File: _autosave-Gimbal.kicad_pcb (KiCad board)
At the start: 2 copper layers, 68.6 x 78.7 mm, 53 parts, among them J1 XT60-M, J3 0022232041, J4 0022232041, J5 0022232041, J6 Conn_01x02, P1 USB_C_Plug, SW1 SW_Push, SW2 SW_Push, U1 ESP32-S2-SOLO, U2 BMI088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

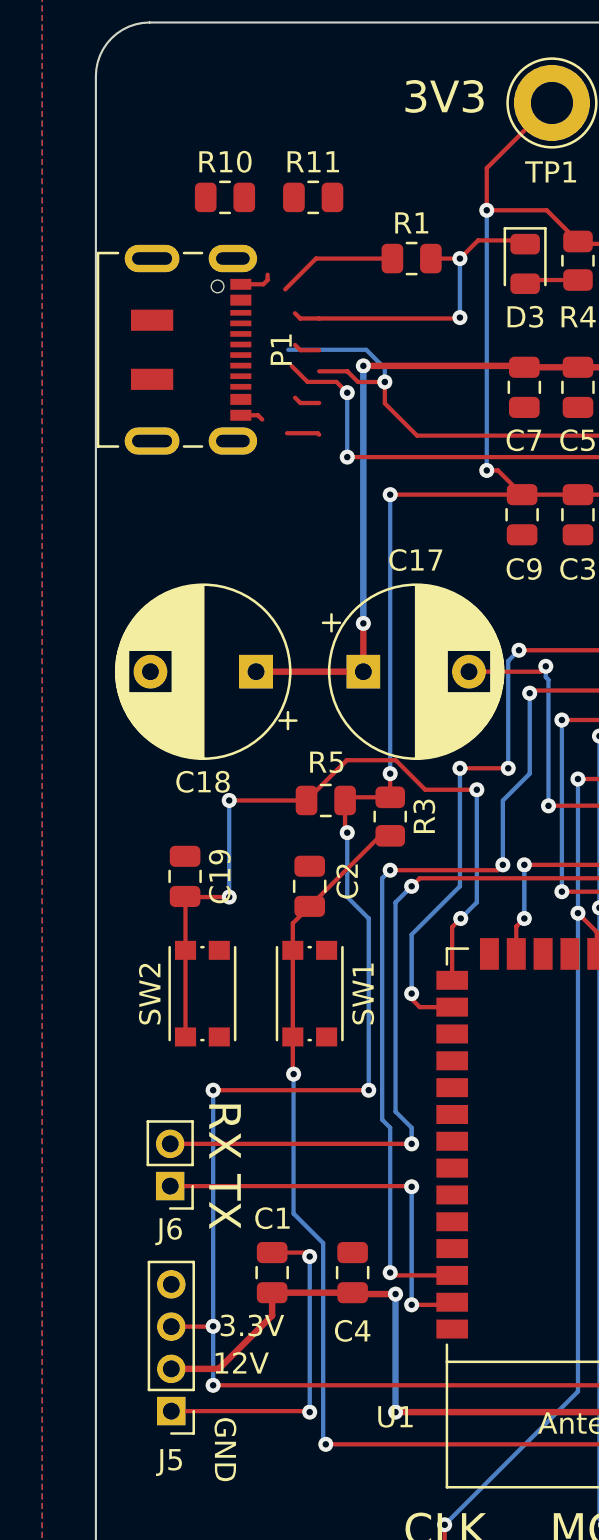
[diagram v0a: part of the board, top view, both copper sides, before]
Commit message: Fixed USB connector issues
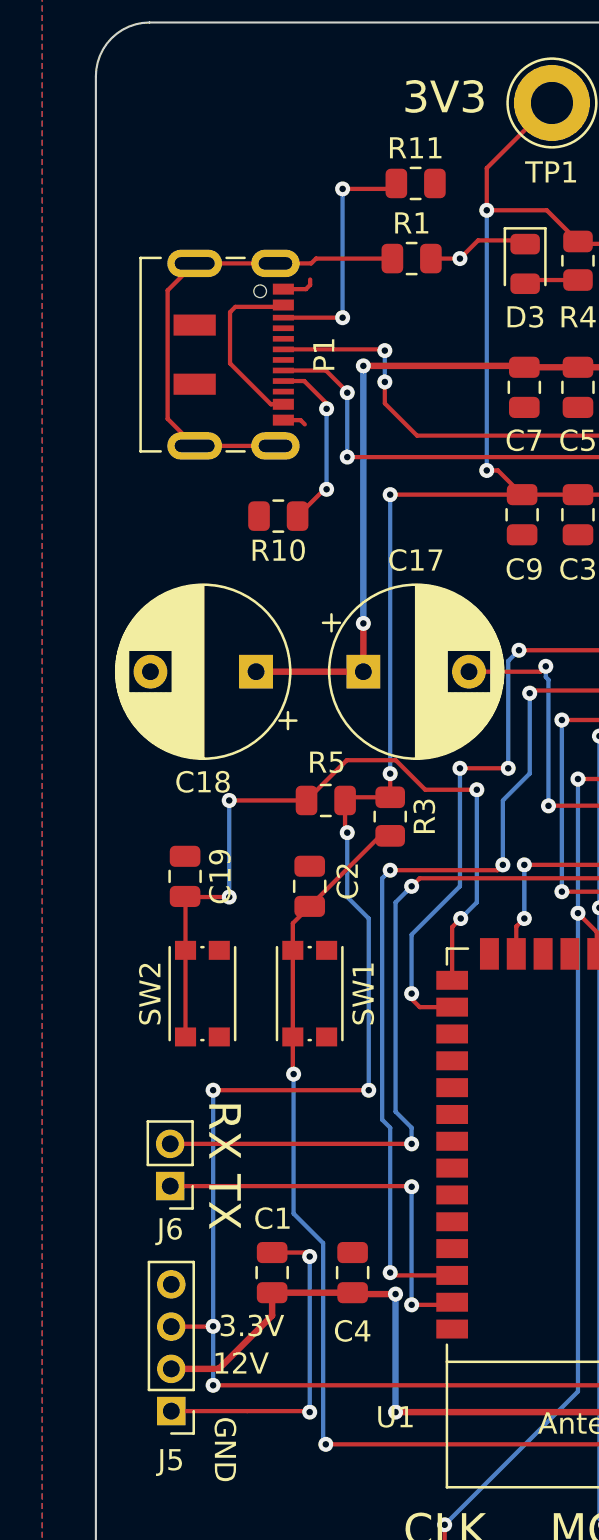
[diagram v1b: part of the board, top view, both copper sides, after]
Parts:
- moved R10 15.3 mm to (122.9, 69.1), turned to 180 degrees
- moved R11 4.89 mm to (129.4, 53.3)
- moved P1 2.03 mm to (120.1, 61.4)
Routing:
- net Net-(R1-Pad1): track 5.68 -> 23.0 mm
- net GND: track 60.2 -> 45.4 mm, vias 8 -> 7
- net Net-(R11-Pad1): track 0.00 -> 11.6 mm, vias 0 -> 2
- net Net-(R10-Pad1): track 0.00 -> 8.45 mm, vias 0 -> 2
- net unconnected-(P1-PadA4): track 0.00 -> 8.42 mm
- net /D+: track 58.5 -> 55.9 mm, vias 3 -> 4

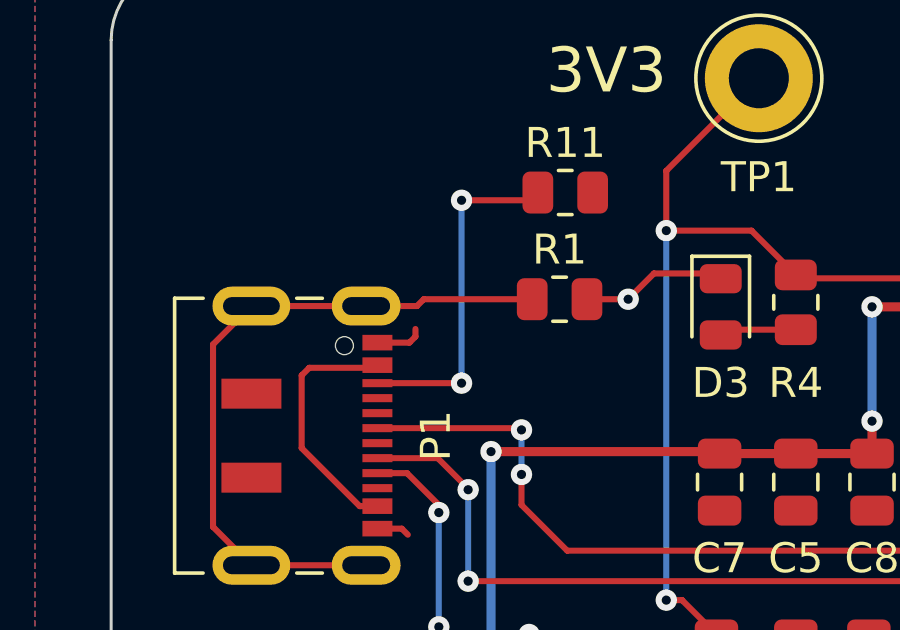
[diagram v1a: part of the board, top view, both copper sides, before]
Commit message: Fixed USB connector issues
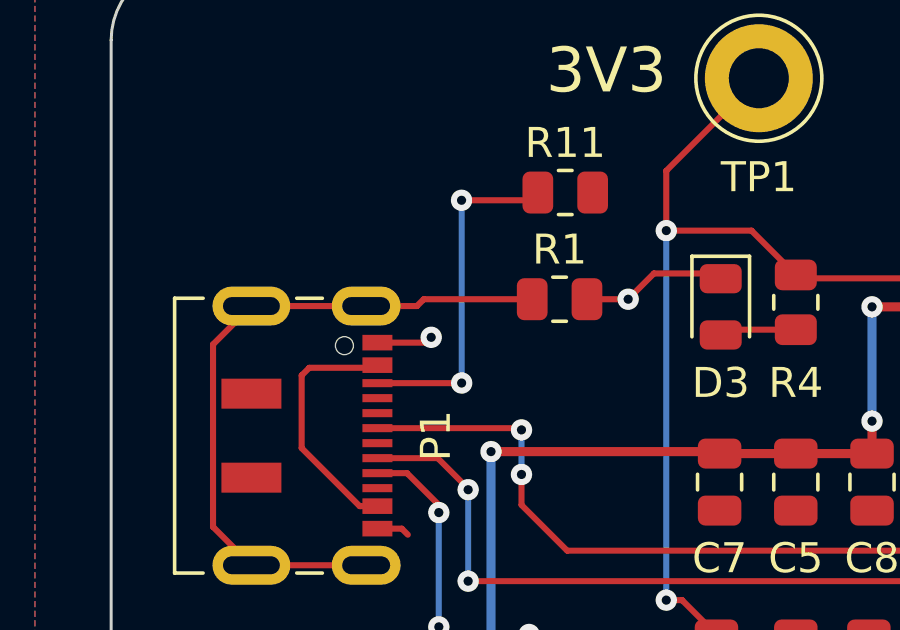
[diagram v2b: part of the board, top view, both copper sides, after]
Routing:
- net GND: track 45.4 -> 45.7 mm, vias 7 -> 8
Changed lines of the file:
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@@
   (segment (start 135.598 76.2) (end 135.344 76.454) (width 0.2032) (layer "F.Cu") (net 2))
   (segment (start 141.186 82.326) (end 141.186 82.7965) (width 0.2032) (layer "F.Cu") (net 2))
+  (segment (start 123.1755 58.344) (end 124.79 58.344) (width 0.2032) (layer "F.Cu") (net 2))
   (segment (start 140.186 82.2558) (end 140.2368 82.205) (width 0.2032) (layer "F.Cu") (net 2))
   (segment (start 141.065 82.205) (end 141.186 82.326) (width 0.2032) (layer "F.Cu") (net 2))
@@
   (segment (start 122.644 103.952) (end 124.234 103.952) (width 0.2032) (layer "F.Cu") (net 2))
   (segment (start 139.686 82.7965) (end 135.8595 82.7965) (width 0.2032) (layer "F.Cu") (net 2))
-  (segment (start 124.4435 58.142) (end 124.2415 58.344) (width 0.2032) (layer "F.Cu") (net 2))
   (segment (start 158.216 107.539) (end 158.216 105.422) (width 0.2032) (layer "F.Cu") (net 2))
   (segment (start 141.186 82.326) (end 141.307 82.205) (width 0.2032) (layer "F.Cu") (net 2))
   (segment (start 134.582 56.037) (end 132.393 56.037) (width 0.2032) (layer "F.Cu") (net 2))
   (segment (start 140.2368 82.205) (end 141.065 82.205) (width 0.2032) (layer "F.Cu") (net 2))
+  (segment (start 124.79 58.344) (end 124.968 58.166) (width 0.2032) (layer "F.Cu") (net 2))
   (segment (start 155.684 110.724) (end 155.664 110.744) (width 0.2032) (layer "F.Cu") (net 2))
   (segment (start 121.46 111.458) (end 124.374 111.458) (width 0.2032) (layer "F.Cu") (net 2))
@@
   (segment (start 140.186 82.7965) (end 140.186 82.2558) (width 0.2032) (layer "F.Cu") (net 2))
   (segment (start 123.9875 64.544) (end 124.1895 64.746) (width 0.2032) (layer "F.Cu") (net 2))
-  (segment (start 124.2415 58.344) (end 123.1755 58.344) (width 0.2032) (layer "F.Cu") (net 2))
-  (segment (start 124.4435 58.142) (end 124.4435 57.888) (width 0.2032) (layer "F.Cu") (net 2))
   (segment (start 123.1755 64.544) (end 123.9875 64.544) (width 0.2032) (layer "F.Cu") (net 2))
   (segment (start 158.216 105.422) (end 158.204 105.41) (width 0.2032) (layer "F.Cu") (net 2))
@@
   (segment (start 142.065 82.205) (end 142.186 82.326) (width 0.2032) (layer "F.Cu") (net 2))
   (segment (start 142.186 82.326) (end 142.186 82.7965) (width 0.2032) (layer "F.Cu") (net 2))
+  (via (at 124.968 58.166) (size 0.7112) (drill 0.3048) (layers "F.Cu" "B.Cu") (net 2))
   (via (at 124.422 104.14) (size 0.7112) (drill 0.3048) (layers "F.Cu" "B.Cu") (net 2))
   (via (at 135.598 76.2) (size 0.7112) (drill 0.3048) (layers "F.Cu" "B.Cu") (net 2))
@@
   (segment (start 147.028 69.85) (end 147.028 65.278) (width 0.2) (layer "B.Cu") (net 37))
   (segment (start 127.978 62.738) (end 127.978 62.096237) (width 0.2) (layer "B.Cu") (net 37))
-  (segment (start 128.016 61.214) (end 127.978 61.252) (width 0.2) (layer "B.Cu") (net 37))
   (segment (start 150.838 89.916) (end 150.838 73.66) (width 0.2) (layer "B.Cu") (net 37))
   (segment (start 150.838 73.66) (end 147.028 69.85) (width 0.2) (layer "B.Cu") (net 37))
@@
   (segment (start 125.222 64.008) (end 125.222 67.564) (width 0.2032) (layer "B.Cu") (net 82))
   (segment (start 128.266 53.598) (end 128.524 53.34) (width 0.2032) (layer "F.Cu") (net 83))
-  (segment (start 125.984 59.69) (end 125.98 59.694) (width 0.2032) (layer "F.Cu") (net 83))
+  (segment (start 125.98 59.694) (end 125.984 59.69) (width 0.2032) (layer "F.Cu") (net 83))
   (segment (start 125.98 53.598) (end 128.266 53.598) (width 0.2032) (layer "F.Cu") (net 83))
   (segment (start 123.1755 59.694) (end 125.98 59.694) (width 0.2032) (layer "F.Cu") (net 83))
-  (via (at 125.98 59.694) (size 0.7112) (drill 0.3048) (layers "F.Cu" "B.Cu") (net 83))
+  (via (at 125.984 59.69) (size 0.7112) (drill 0.3048) (layers "F.Cu" "B.Cu") (net 83))
   (via (at 125.98 53.598) (size 0.7112) (drill 0.3048) (layers "F.Cu" "B.Cu") (net 83))
-  (segment (start 125.98 59.694) (end 125.98 53.598) (width 0.2032) (layer "B.Cu") (net 83))
-  (segment (start 125.984 53.594) (end 125.98 53.598) (width 0.2032) (layer "B.Cu") (net 83))
+  (segment (start 125.984 59.69) (end 125.984 53.602) (width 0.2032) (layer "B.Cu") (net 83))
+  (segment (start 125.984 53.602) (end 125.98 53.598) (width 0.2032) (layer "B.Cu") (net 83))
   (segment (start 123.1755 59.094) (end 123.0875 59.182) (width 0.2032) (layer "F.Cu") (net 84))
   (segment (start 122.585139 63.794) (end 123.1755 63.794) (width 0.2032) (layer "F.Cu") (net 84))
